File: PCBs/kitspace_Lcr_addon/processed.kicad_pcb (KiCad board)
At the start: 2 copper layers, 85.1 x 55.1 mm, 17 parts, among them J2 LCr_ conector, J4 blank in, J5 Green control output, J6 Blue control output, J7 Red control output, J8 blank_jumper, U1 SN74LS08N, U2 SN74LS08N, U3 SN74HC14N, U4 LM2596T-5

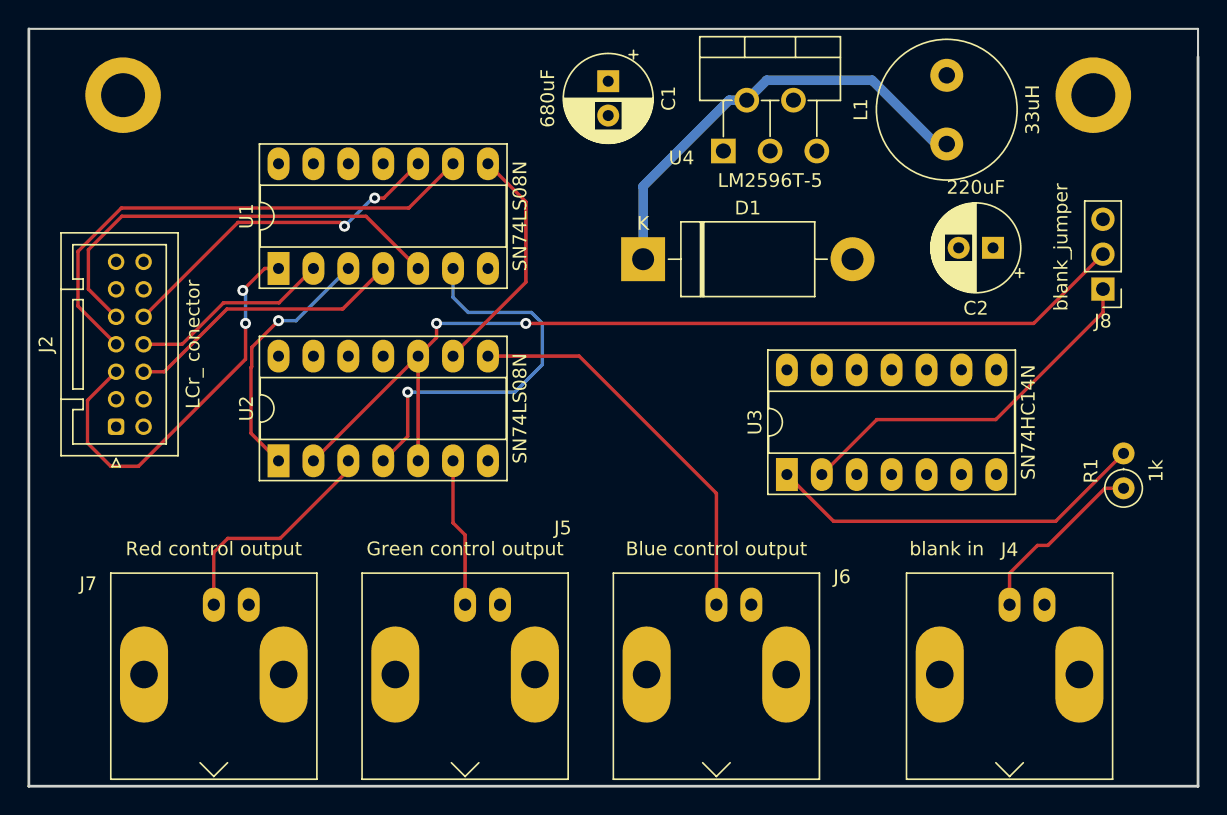
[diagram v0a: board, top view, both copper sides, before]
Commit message: recheck all circuits and clean up fill zone by rerouting the nets using freerouting and manually
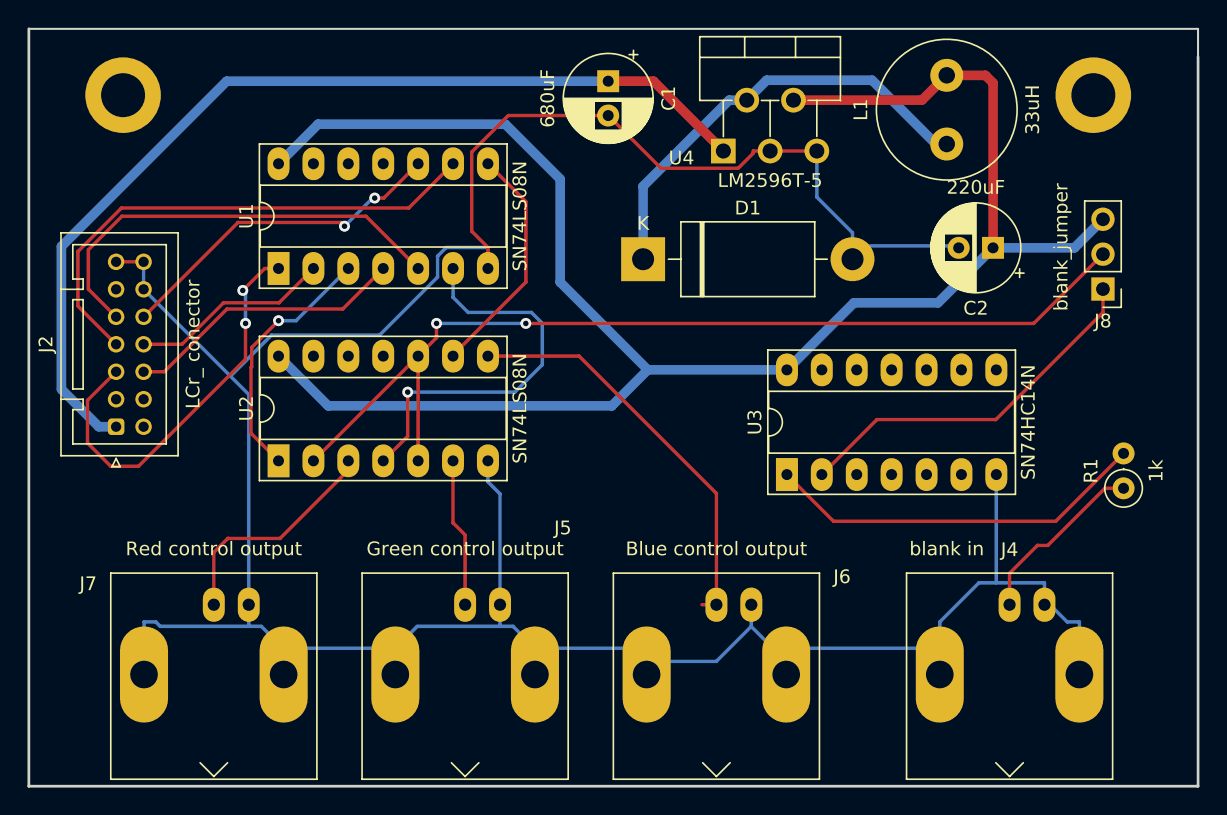
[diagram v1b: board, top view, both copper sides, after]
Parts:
- renumbered REF** to REF**_2
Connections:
- C1 pad 1: (no net) -> +12V
- C1 pad 2: (no net) -> GND
- C2 pad 1: (no net) -> +5V
- C2 pad 2: (no net) -> GND
- D1 pad 2: (no net) -> GND
- J2 pad 1: (no net) -> +12V
- J2 pad 12: (no net) -> GND
- J2 pad 13: (no net) -> GND
- J2 pad 14: (no net) -> GND
- J4 pad 2: (no net) -> GND
- J5 pad 2: (no net) -> GND
- J6 pad 2: (no net) -> GND
- J7 pad 2: (no net) -> GND
- J8 pad 3: (no net) -> +5V
- L1 pad 2: (no net) -> +5V
- U1 pad 14: (no net) -> +5V
- U1 pad 7: (no net) -> GND
- U2 pad 14: (no net) -> +5V
- U2 pad 7: (no net) -> GND
- U3 pad 14: (no net) -> +5V
- U3 pad 4: (no net) -> Net-(U3-Pad4)
- U3 pad 7: (no net) -> GND
- U4 pad 1: (no net) -> +12V
- U4 pad 3: (no net) -> GND
- U4 pad 4: (no net) -> +5V
- U4 pad 5: (no net) -> GND
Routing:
- net GND: track 0.00 -> 229.5 mm
- net +5V: track 0.00 -> 134.5 mm
- net +12V: track 0.00 -> 70.8 mm
- net Net-(J6-Pad1): track 28.9 -> 29.9 mm
